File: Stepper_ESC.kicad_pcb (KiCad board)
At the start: 4 copper layers, 125 x 60 mm, 202 parts, among them J1 12V_Input, J2 Conn_01x05, J4 Screw_Terminal_01x02, J5 BLR-514-5-V, J6 BLR-514-5-V, J7 BLR-514-5-V, J8 BLR-514-5-V, Q10 MCM3400A-TP, Q11 MCM3400A-TP, Q12 MCM3400A-TP, Q13 MCM3400A-TP, Q14 MCM3400A-TP, Q15 MCM3400A-TP, Q16 MCM3400A-TP, Q17 MCM3400A-TP, Q18 MCM3400A-TP, Q19 MCM3400A-TP, Q20 MCM3400A-TP, Q5 MCM3400A-TP, Q6 MCM3400A-TP, Q7 MCM3400A-TP, Q8 MCM3400A-TP, Q9 MCM3400A-TP, U1 TPS54360DDA, U10 TMC5160A-TA-T, U2 AMS1117-3.3, U3 STM32G474RETx, U5 TCAN1473-Q1, U6 AS5047P-ATSM, U7 TMC5160A-TA-T, U8 TMC5160A-TA-T, U9 TMC5160A-TA-T, Y1 ECS-80-12-33-JGN-TR3

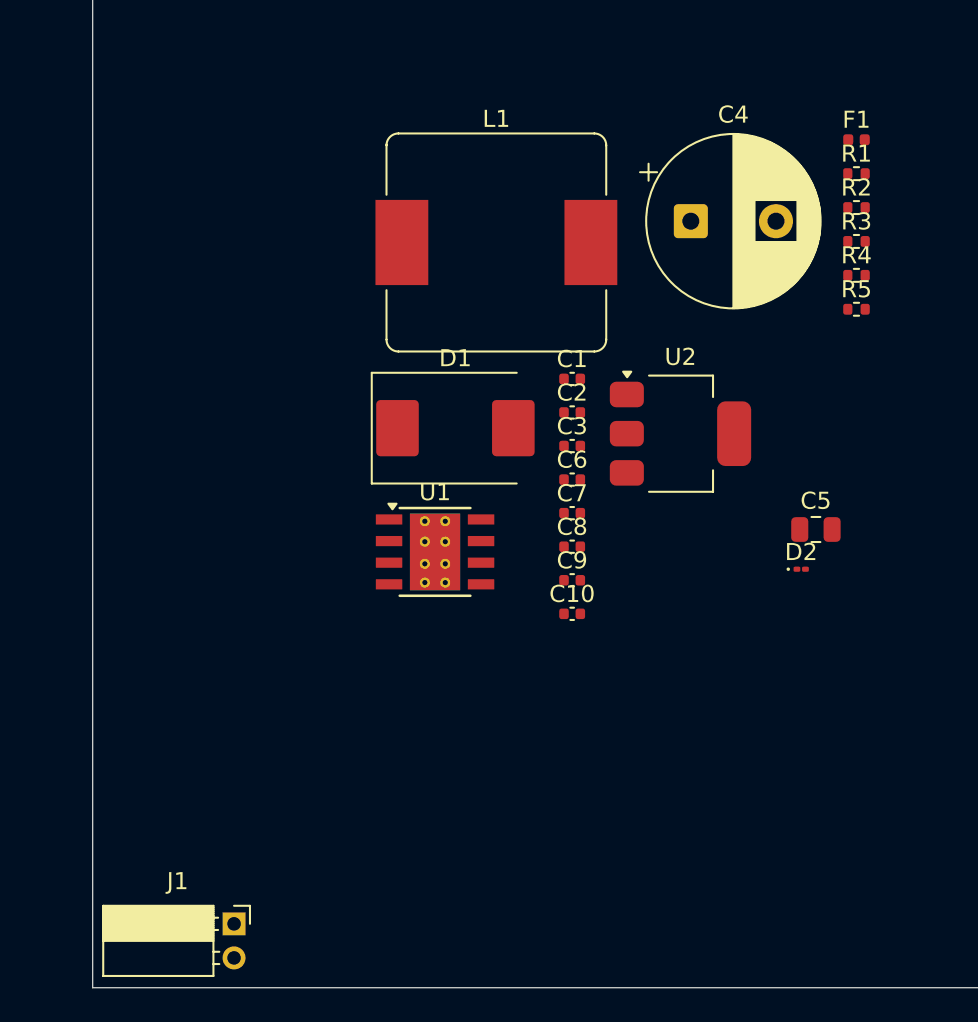
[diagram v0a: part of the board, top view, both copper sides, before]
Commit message: Updated traces on PCB for the power supply, added XT60PW power connector for the board.
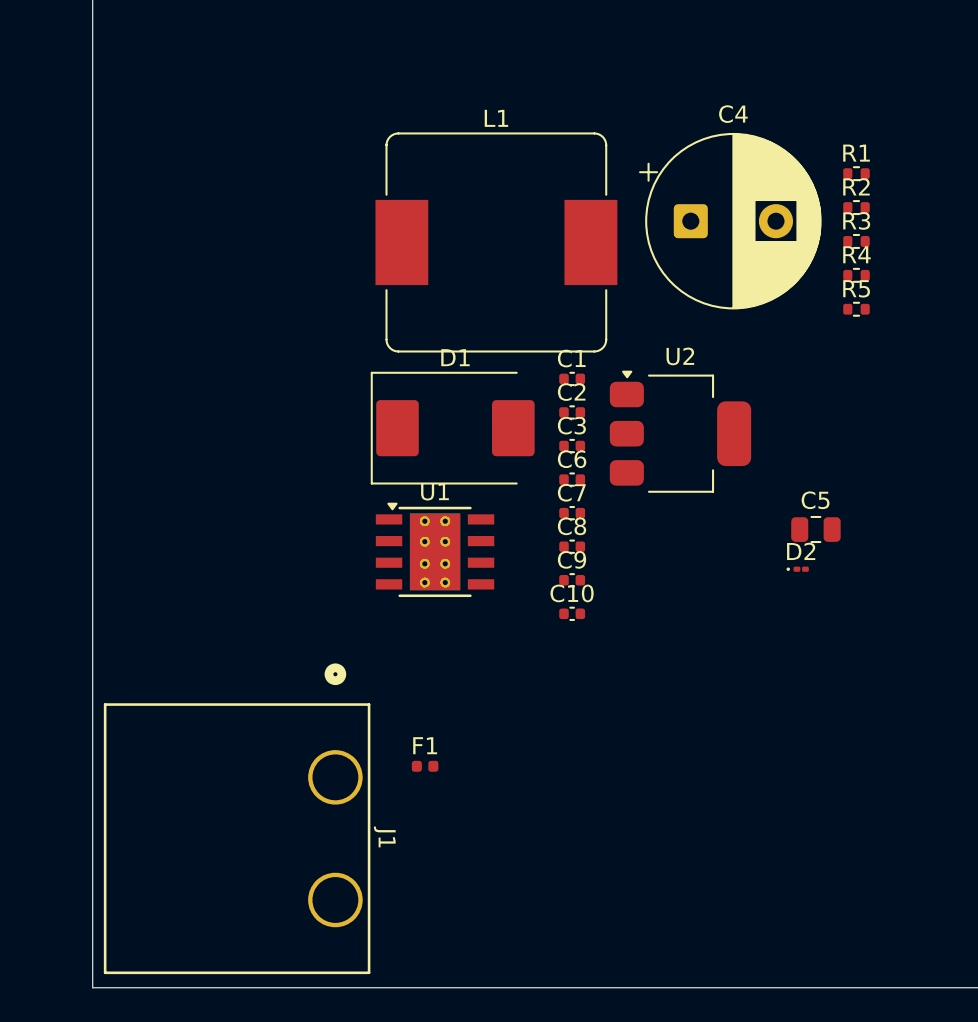
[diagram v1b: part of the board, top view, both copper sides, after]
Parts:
- J1: value 12V_Input -> XT60PW-M; footprint Connector_PinSocket_2.00mm:PinSocket_1x02_P2.00mm_Horizontal -> Stepper_ESC:CONN_XT60PW-M_AMA
- moved F1 44.7 mm to (95.0, 97.8)
- moved J1 10.5 mm to (89.8, 98.4), turned to -90 degrees
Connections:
- F1 pad 2: Net-(J1-Pin_1) -> Net-(F1-Pad2)
- J1 pad 1: Net-(J1-Pin_1) -> GND
- J1 pad 2: GND -> Net-(F1-Pad2)

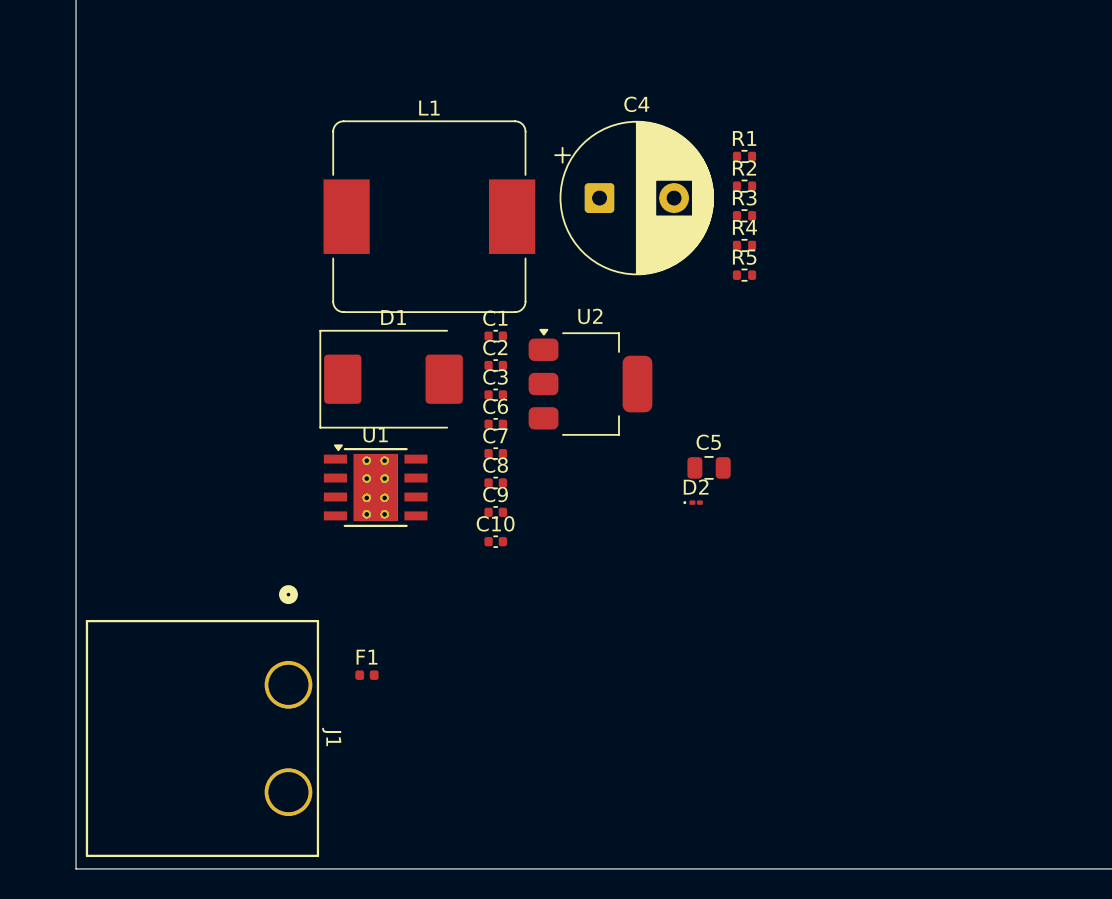
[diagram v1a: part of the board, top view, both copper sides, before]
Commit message: Added Fuse holder and diode footprints
Signed-off-by: Vincent Cadicamo <vcadicamo@icloud.com>
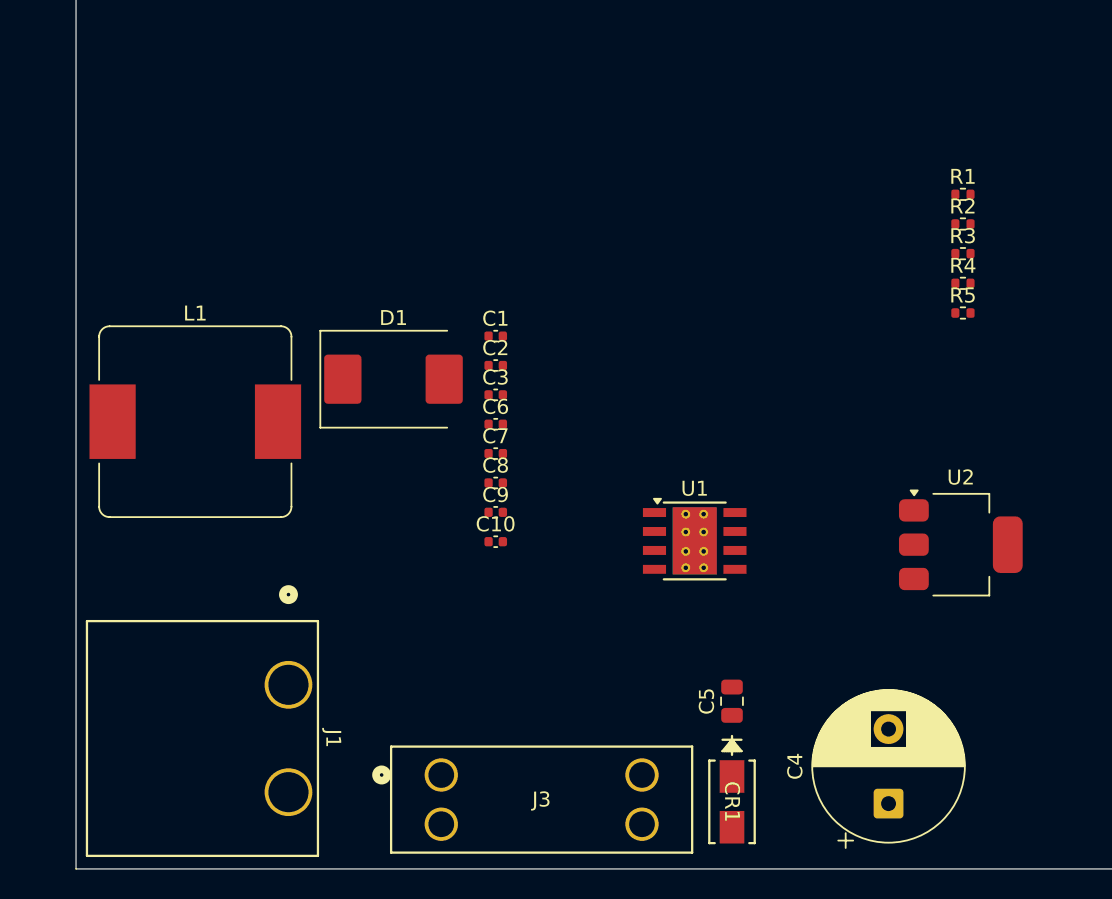
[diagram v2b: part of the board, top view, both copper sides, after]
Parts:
- removed D2: SMBJ15A, Diode_SMD:D_01005_0402Metric
- removed F1: 15A, Fuse:Fuse_0402_1005Metric
- added CR1: SMCJ15A, Stepper_ESC:DIODE_DO-214AC, F.Cu at (119.5, 106.2)
- added J3: 3557-2, Stepper_ESC:CONN_3557-2_KEY, F.Cu at (100.0, 104.4)
- moved C4 45.0 mm to (130.0, 106.4), turned to 90 degrees
- moved U2 27.1 mm to (134.8, 89.0)
- moved U1 21.7 mm to (117.0, 88.8)
- moved L1 20.9 mm to (83.5, 80.8)
- moved C5 15.7 mm to (119.5, 99.5), turned to 90 degrees
- moved R1 14.9 mm to (135.0, 65.5)
- moved R2 14.9 mm to (135.0, 67.5)
- moved R3 14.9 mm to (135.0, 69.5)
- moved R4 14.9 mm to (135.0, 71.5)
- moved R5 14.9 mm to (135.0, 73.5)

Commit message: Updated Traces from power regulators to power connector to the board.
Signed-off-by: Vincent Cadicamo <vcadicamo@icloud.com>
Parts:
- moved C10 39.1 mm to (139.5, 73.2)
- moved C8 39.1 mm to (139.5, 69.2)
- moved C9 39.1 mm to (139.5, 71.2)
- moved R1 35.6 mm to (105.5, 85.5)
- moved R2 33.9 mm to (105.5, 84.2)
- moved L1 30.2 mm to (112.5, 72.5)
- moved C2 29.4 mm to (132.5, 71.5)
- moved C3 29.4 mm to (132.5, 73.5)
- moved R3 24.3 mm to (117.0, 85.8)
- moved R4 22.2 mm to (117.0, 84.5)
- moved R5 20.5 mm to (117.0, 83.2)
- moved U2 13.8 mm to (148.5, 91.0)
- moved C7 13.4 mm to (117.0, 82.0), turned to 180 degrees
- moved C6 13.4 mm to (117.0, 80.8)
- moved U1 8.02 mm to (110.8, 83.6)
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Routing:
- net Net-(U1-COMP): track 0.00 -> 8.79 mm
- net GND: track 0.00 -> 6.25 mm, vias 0 -> 4
- net Net-(U1-FB): track 0.00 -> 4.70 mm
- net Net-(U1-EN): track 0.00 -> 2.15 mm
- net Net-(U1-BOOT): track 0.00 -> 2.14 mm
- net Net-(U1-RT/CLK): track 0.00 -> 2.14 mm
- net Net-(C7-Pad1): track 0.00 -> 1.25 mm
